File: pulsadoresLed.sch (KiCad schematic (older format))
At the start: 8 parts

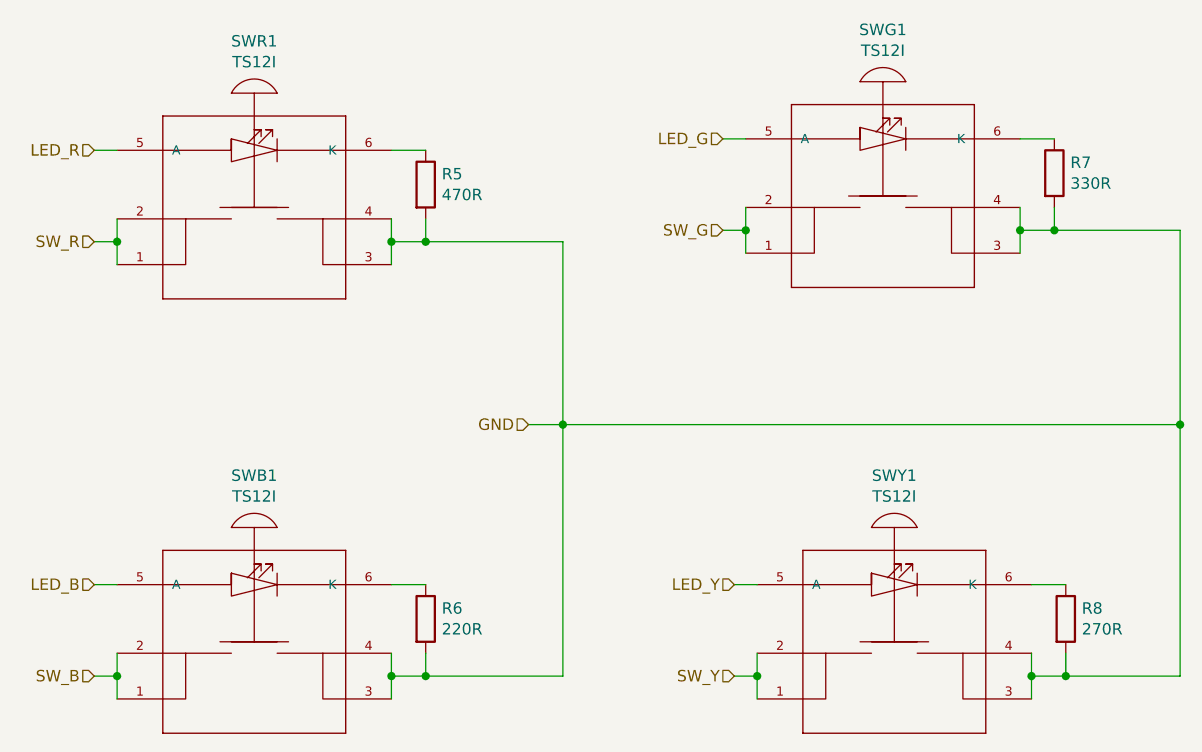
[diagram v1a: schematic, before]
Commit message: Se aplicaron correciones indicadas por el profesor en el esquemático
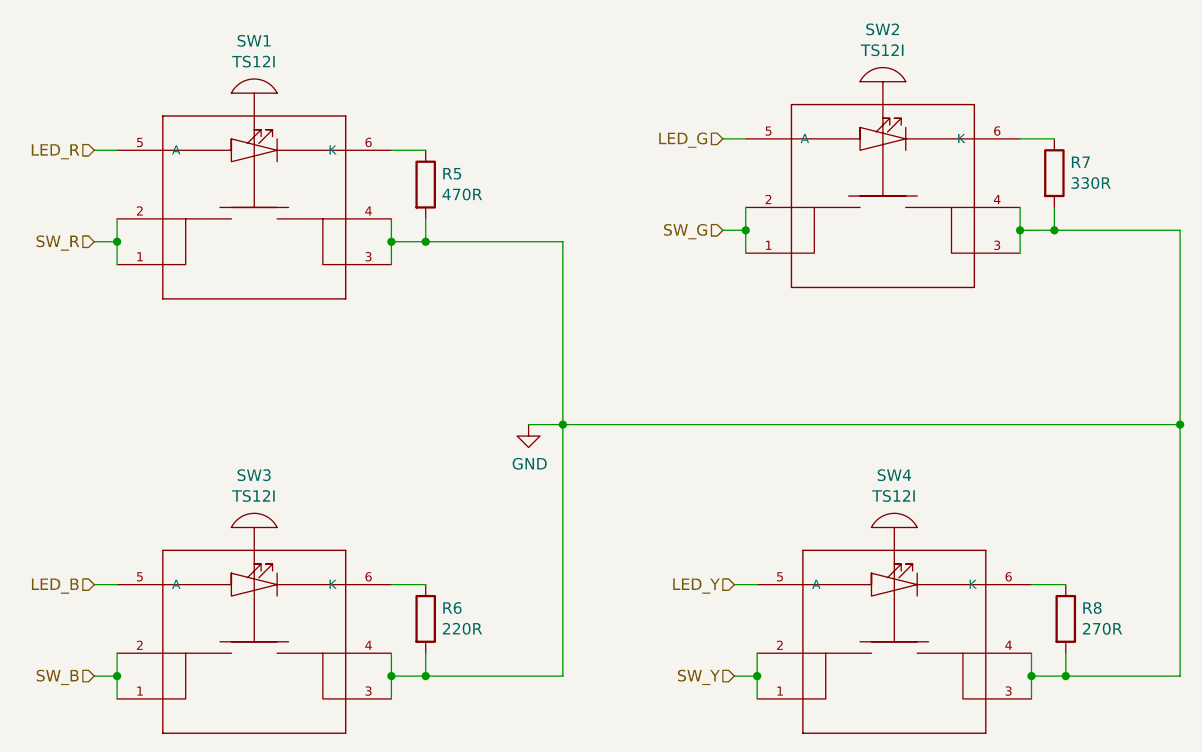
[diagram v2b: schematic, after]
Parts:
- renumbered SWR1 to SW1, SWG1 to SW2, SWB1 to SW3, SWY1 to SW4
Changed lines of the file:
@@
 $Descr A4 11693 8268
 encoding utf-8
-Sheet 6 6
+Sheet 3 4
 Title "Sistema de comunicación en tiempo real por mensajes de voz
 "
@@
 Rev "1.0"
 Comp "Marcelo Pistarelli"
-Comment1 ""
+Comment1 "<C> 2018 Todos los derechos reservados"
 Comment2 ""
 Comment3 ""
@@
 $EndDescr
 $Comp
-L tpfinal:TS12I SWR1
+L tpfinal:TS12I SW1
 U 1 1 5BC6F482
 P 4200 2750
-F 0 "SWR1" H 4200 3477 50  0000 C CNN
+F 0 "SW1" H 4200 3477 50  0000 C CNN
 F 1 "TS12I" H 4200 3386 50  0000 C CNN
 F 2 "tpfinal:TS12I" H 3500 2000 50  0001 L BNN
@@
 $EndComp
 $Comp
-L tpfinal:TS12I SWG1
+L tpfinal:TS12I SW2
 U 1 1 5BC6F666
 P 6950 2700
-F 0 "SWG1" H 6950 3427 50  0000 C CNN
+F 0 "SW2" H 6950 3427 50  0000 C CNN
 F 1 "TS12I" H 6950 3336 50  0000 C CNN
 F 2 "tpfinal:TS12I" H 6250 1950 50  0001 L BNN
@@
 $EndComp
 $Comp
-L tpfinal:TS12I SWB1
+L tpfinal:TS12I SW3
 U 1 1 5BC6F760
 P 4200 4650
-F 0 "SWB1" H 4200 5377 50  0000 C CNN
+F 0 "SW3" H 4200 5377 50  0000 C CNN
 F 1 "TS12I" H 4200 5286 50  0000 C CNN
 F 2 "tpfinal:TS12I" H 3500 3900 50  0001 L BNN
@@
 $EndComp
 $Comp
-L tpfinal:TS12I SWY1
+L tpfinal:TS12I SW4
 U 1 1 5BC6F7CF
 P 7000 4650
-F 0 "SWY1" H 7000 5377 50  0000 C CNN
+F 0 "SW4" H 7000 5377 50  0000 C CNN
 F 1 "TS12I" H 7000 5286 50  0000 C CNN
 F 2 "tpfinal:TS12I" H 6300 3900 50  0001 L BNN
@@
 Wire Wire Line
 	6300 4400 6400 4400
-Text HLabel 5400 3700 0    50   Input ~ 0
-GND
 Wire Wire Line
 	5400 3700 5550 3700
@@
 Wire Wire Line
 	6400 4800 6400 4900
+$Comp
+L power:GND #PWR0103
+U 1 1 5BFAD7C5
+P 5400 3700
+F 0 "#PWR0103" H 5400 3450 50  0001 C CNN
+F 1 "GND" H 5405 3527 50  0000 C CNN
+F 2 "" H 5400 3700 50  0001 C CNN
+F 3 "" H 5400 3700 50  0001 C CNN
+	1    5400 3700
+	1    0    0    -1
+$EndComp
 $EndSCHEMATC
